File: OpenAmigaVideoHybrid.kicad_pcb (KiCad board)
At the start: 2 copper layers, 56.4 x 21.1 mm, 52 parts, among them J1 Conn_01x22, J99 OSHW_LOGO, Q1 2N3904, Q2 2N3904, Q3 2N3904, Q4 2N3904, Q5 2N3904, Q6 2N3906

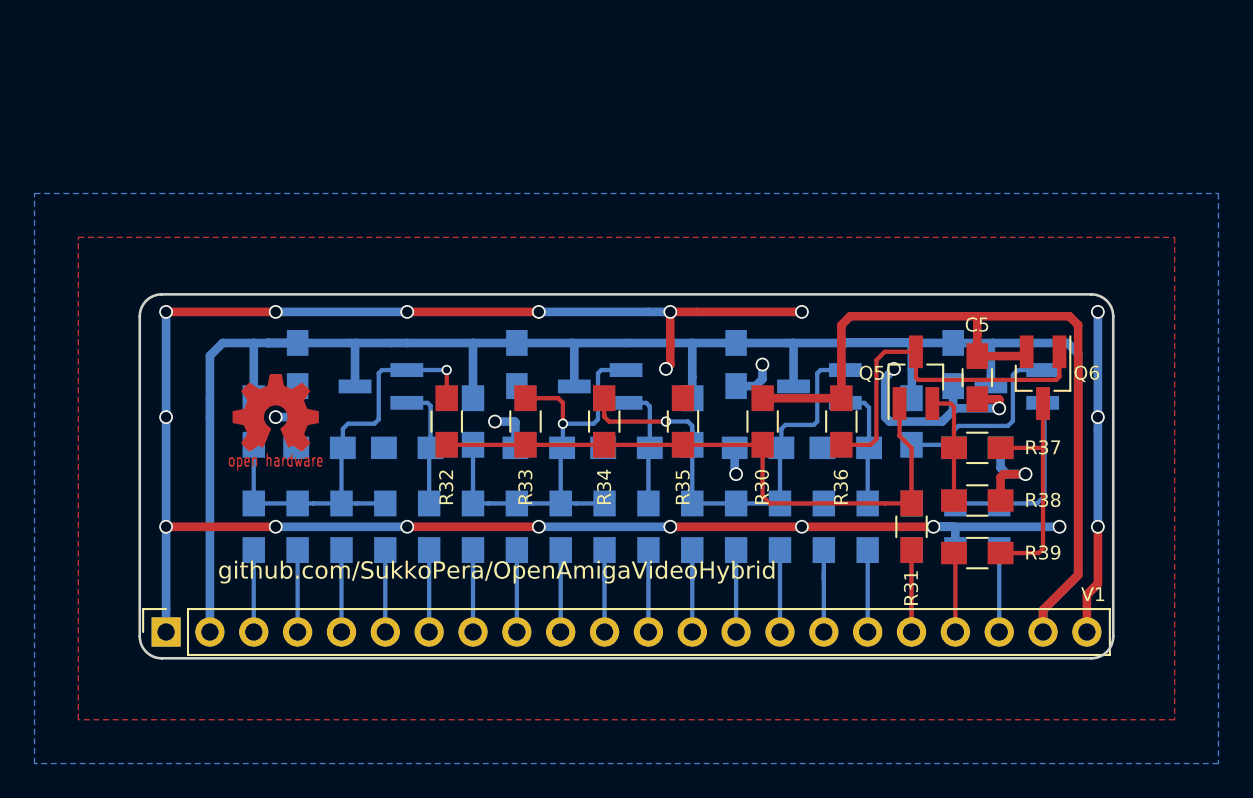
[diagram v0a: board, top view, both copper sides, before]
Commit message: Begin migrating project to KiCad 5
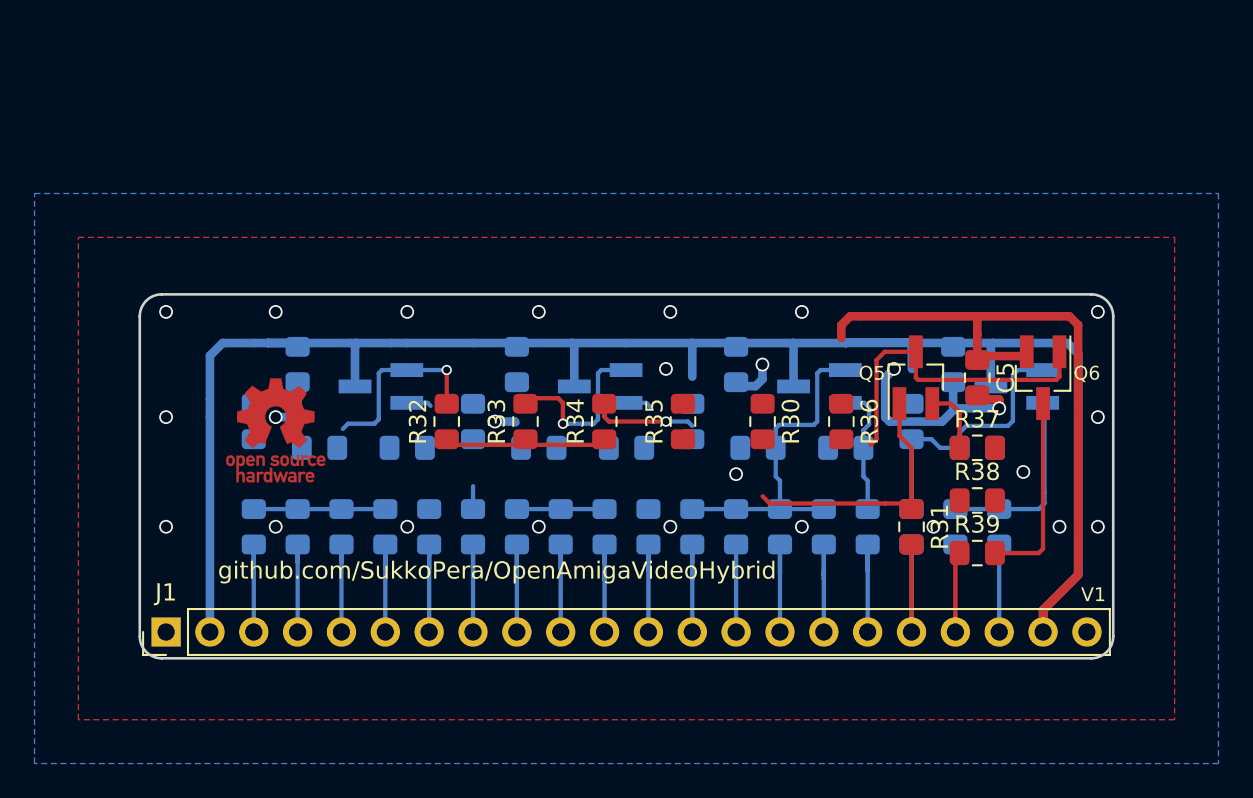
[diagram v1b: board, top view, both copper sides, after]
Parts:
- removed J99: OSHW_LOGO, w_logo:Logo_copper_OSHW_6x6mm
- added V0: OSHW_LOGO, Symbol:OSHW-Logo_5.7x6mm_Copper, F.Cu at (125.7, 112.8)
- C1, C2, C3, C4, C5: footprint Capacitors_SMD:C_0805_HandSoldering -> Capacitor_SMD:C_0805_2012Metric_Pad1.15x1.40mm_HandSolder
- J1: value Conn_01x22 -> CONN_MAINBOARD; footprint OpenAmigaVideoHybrid:Pin_Header_Straight_1x22_Pitch2.54mm -> Connector_PinHeader_2.54mm:PinHeader_1x22_P2.54mm_Vertical; moved to F.Cu
- R1, R10, R11, R12, R13, R14, R15, R16, R17, R18, R19, R2, R20, R21, R22, R23, R24, R25, R26, R27, R28, R29, R3, R30, R31, R32, R33, R34, R35, R36, R37, R38, R39, R4, R5, R6, R7, R8, R9: footprint Resistors_SMD:R_0805_HandSoldering -> Resistor_SMD:R_0805_2012Metric_Pad1.15x1.40mm_HandSolder
- turned J1 to 90 degrees
- turned R22 to 0 degrees
- turned R23 to 0 degrees
- turned R25 to 90 degrees
- turned R27 to 180 degrees
- turned R28 to 90 degrees
- turned R37 to 0 degrees
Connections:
- R13 pad 1: VCC -> Net-(Q2-Pad2)
- R13 pad 2: Net-(Q2-Pad2) -> VCC
- R14 pad 1: Net-(Q2-Pad2) -> GND
- R14 pad 2: GND -> Net-(Q2-Pad2)
- R15 pad 1: Net-(Q2-Pad1) -> GND
- R15 pad 2: GND -> Net-(Q2-Pad1)
- R21 pad 1: VCC -> Net-(Q3-Pad2)
- R21 pad 2: Net-(Q3-Pad2) -> VCC
- R22 pad 1: Net-(Q3-Pad2) -> GND
- R22 pad 2: GND -> Net-(Q3-Pad2)
- R23 pad 1: Net-(Q3-Pad1) -> GND
- R23 pad 2: GND -> Net-(Q3-Pad1)
- R25 pad 1: VCC -> Net-(Q4-Pad2)
- R25 pad 2: Net-(Q4-Pad2) -> VCC
- R27 pad 1: Net-(Q4-Pad2) -> GND
- R27 pad 2: GND -> Net-(Q4-Pad2)
- R28 pad 1: Net-(Q4-Pad1) -> GND
- R28 pad 2: GND -> Net-(Q4-Pad1)
- R30 pad 1: VCC -> Net-(Q5-Pad2)
- R30 pad 2: Net-(Q5-Pad2) -> VCC
- R35 pad 1: Net-(Q5-Pad2) -> GND
- R35 pad 2: GND -> Net-(Q5-Pad2)
- R36 pad 1: VCC -> Net-(Q5-Pad3)
- R36 pad 2: Net-(Q5-Pad3) -> VCC
- R37 pad 1: Net-(Q6-Pad3) -> Net-(Q5-Pad1)
- R37 pad 2: Net-(Q5-Pad1) -> Net-(Q6-Pad3)
- R38 pad 1: Net-(Q5-Pad1) -> GND
- R38 pad 2: GND -> Net-(Q5-Pad1)
- R5 pad 1: VCC -> Net-(Q1-Pad2)
- R5 pad 2: Net-(Q1-Pad2) -> VCC
- R6 pad 1: Net-(Q1-Pad2) -> GND
- R6 pad 2: GND -> Net-(Q1-Pad2)
- R7 pad 1: Net-(Q1-Pad1) -> GND
- R7 pad 2: GND -> Net-(Q1-Pad1)
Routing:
- net GND: track 160.8 -> 19.7 mm
- net VCC: track 159.2 -> 141.8 mm
- net Net-(Q5-Pad2): track 36.1 -> 24.0 mm
- net Net-(Q2-Pad2): track 25.7 -> 16.1 mm
- net Net-(Q1-Pad2): track 26.2 -> 18.5 mm
- net Net-(Q1-Pad1): track 7.13 -> 1.45 mm
- net Net-(Q2-Pad1): track 7.11 -> 1.46 mm
- net Net-(Q3-Pad2): track 30.5 -> 25.9 mm
- net Net-(Q5-Pad1): track 6.75 -> 3.84 mm
- net Net-(Q6-Pad3): track 13.4 -> 11.0 mm
- net /db0: track 5.19 -> 6.96 mm
- net Net-(Q5-Pad3): track 20.6 -> 18.9 mm
- net /db1: track 4.49 -> 6.13 mm
- net /csync: track 9.24 -> 10.9 mm
- net /green: track 4.49 -> 6.01 mm
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
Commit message: Start working on color composite version
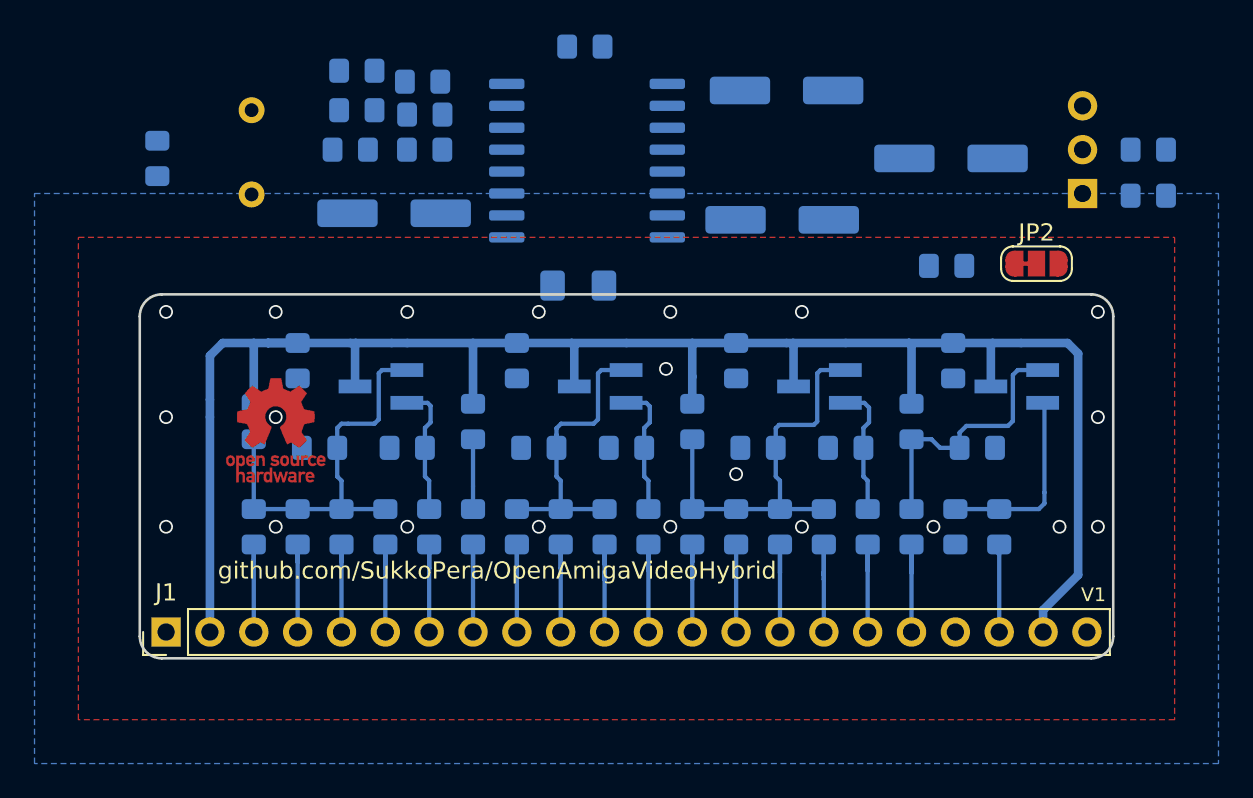
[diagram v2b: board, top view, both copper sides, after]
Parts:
- removed C5: 100n, Capacitor_SMD:C_0805_2012Metric_Pad1.15x1.40mm_HandSolder
- removed Q5: 2N3904, OpenAmigaVideoHybrid:2N3904_2N3906_SOT-23
- removed Q6: 2N3906, OpenAmigaVideoHybrid:2N3904_2N3906_SOT-23
- removed R30: 90.9k, Resistor_SMD:R_0805_2012Metric_Pad1.15x1.40mm_HandSolder
- removed R31, R34: 37.4k, Resistor_SMD:R_0805_2012Metric_Pad1.15x1.40mm_HandSolder
- removed R32: 13.3k, Resistor_SMD:R_0805_2012Metric_Pad1.15x1.40mm_HandSolder
- removed R33: 6.04k, Resistor_SMD:R_0805_2012Metric_Pad1.15x1.40mm_HandSolder
- removed R35: 19.6k, Resistor_SMD:R_0805_2012Metric_Pad1.15x1.40mm_HandSolder
- removed R36: 220, Resistor_SMD:R_0805_2012Metric_Pad1.15x1.40mm_HandSolder
- removed R37, R38: 36, Resistor_SMD:R_0805_2012Metric_Pad1.15x1.40mm_HandSolder
- removed R39: 75, Resistor_SMD:R_0805_2012Metric_Pad1.15x1.40mm_HandSolder
- added C11: 10pF, Capacitor_SMD:C_0805_2012Metric_Pad1.15x1.40mm_HandSolder, B.Cu at (118.9, 97.0)
- added C12: 100n, Capacitor_SMD:C_0805_2012Metric_Pad1.15x1.40mm_HandSolder, B.Cu at (134.4, 96.5)
- added C13: 100n, Capacitor_SMD:C_0805_2012Metric_Pad1.15x1.40mm_HandSolder, B.Cu at (134.4, 94.5)
- added C14: 100n, Capacitor_SMD:C_0805_2012Metric_Pad1.15x1.40mm_HandSolder, B.Cu at (134.2, 92.6)
- added C15: 220u, Capacitor_SMD:CP_Elec_6.3x7.7, B.Cu at (164.8, 97.0)
- added C16: 220u, Capacitor_SMD:CP_Elec_6.3x7.7, B.Cu at (155.1, 100.6)
- added C17: 220u, Capacitor_SMD:CP_Elec_6.3x7.7, B.Cu at (155.3, 93.1)
- added C18: 100n, Capacitor_SMD:C_0805_2012Metric_Pad1.15x1.40mm_HandSolder, B.Cu at (143.6, 90.6)
- added C19: 100u, Capacitor_SMD:CP_Elec_6.3x5.8, B.Cu at (132.6, 100.2)
- added C20: 100n, Capacitor_SMD:C_1206_3216Metric_Pad1.42x1.75mm_HandSolder, B.Cu at (143.3, 104.4)
- added J2: SVIDEO_OUT, Connector_PinHeader_2.54mm:PinHeader_1x03_P2.54mm_Vertical, B.Cu at (172.5, 99.1)
- added JP2: NTSC/~PAL, OpenAmigaVideoHybrid:SolderJumper-3_P1.3mm_Bridged12_RoundedPad1.0x1.5mm, F.Cu at (169.8, 103.1)
- added R40: 75, Resistor_SMD:R_0805_2012Metric_Pad1.15x1.40mm_HandSolder, B.Cu at (130.0, 96.5)
- added R41: 75, Resistor_SMD:R_0805_2012Metric_Pad1.15x1.40mm_HandSolder, B.Cu at (130.4, 94.2)
- added R42: 75, Resistor_SMD:R_0805_2012Metric_Pad1.15x1.40mm_HandSolder, B.Cu at (130.4, 91.9)
- added R43: 75, Resistor_SMD:R_0805_2012Metric_Pad1.15x1.40mm_HandSolder, B.Cu at (164.6, 103.3)
- added R44: 75, Resistor_SMD:R_0805_2012Metric_Pad1.15x1.40mm_HandSolder, B.Cu at (176.3, 99.2)
- added R45: 75, Resistor_SMD:R_0805_2012Metric_Pad1.15x1.40mm_HandSolder, B.Cu at (176.3, 96.5)
- added U2: AD724, Package_SO:SOIC-16W_7.5x10.3mm_P1.27mm, B.Cu at (143.8, 97.2)
- added Y2: 4.433619M, Crystal:Crystal_HC49-4H_Vertical, B.Cu at (124.3, 94.2)
- moved C1 0.22 mm to (127.0, 108.7)
- moved C2 0.22 mm to (139.7, 108.7)
- moved C3 0.22 mm to (152.4, 108.7)
- moved C4 0.22 mm to (165.0, 108.7)
- turned R13 to 90 degrees
- turned R14 to 0 degrees
- turned R15 to 0 degrees
- turned R21 to 90 degrees
- turned R5 to 90 degrees
- turned R6 to 0 degrees
- turned R7 to 0 degrees
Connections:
- net VCC renamed VAA
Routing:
- net VAA: track 141.8 -> 109.7 mm
- net Net-(Q5-Pad2): track 24.0 -> 0.00 mm
- net GND: track 19.7 -> 0.11 mm, vias 26 -> 21
- net Net-(Q5-Pad3): track 18.9 -> 0.00 mm
- net Net-(Q6-Pad3): track 11.0 -> 0.00 mm
- net Net-(Q1-Pad1): track 1.45 -> 7.66 mm
- net Net-(Q2-Pad1): track 1.46 -> 7.64 mm
- net Net-(Q1-Pad2): track 18.5 -> 23.4 mm, vias 1 -> 0
- net /csync: track 10.9 -> 6.13 mm
- net /comp: track 4.61 -> 0.00 mm
- net Net-(Q2-Pad2): track 16.1 -> 20.6 mm, vias 1 -> 0
- net Net-(Q5-Pad1): track 3.84 -> 0.00 mm
- net Net-(Q3-Pad2): track 25.9 -> 23.5 mm, vias 1 -> 0

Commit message: Almost there...
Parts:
- C1, C2, C3, C4, Q1, Q2, Q3, Q4, R1, R10, R11, R12, R13, R14, R15, R16, R17, R18, R19, R2, R20, R21, R22, R23, R24, R25, R26, R27, R28, R29, R3, R4, R5, R6, R7, R8, R9: moved to F.Cu
- JP2, V0: moved to B.Cu
- Y2: footprint Crystal:Crystal_HC49-4H_Vertical -> Crystal:Crystal_SMD_HC49-SD
- moved JP2 35.5 mm to (137.9, 118.7), turned to 270 degrees
- moved Y2 26.5 mm to (129.4, 120.3), turned to 0 degrees
- moved C11 23.6 mm to (132.6, 116.2), turned to 180 degrees
- moved C20 22.7 mm to (122.8, 114.3)
- moved C15 22.0 mm to (168.3, 118.7)
- moved C16 18.4 mm to (158.2, 118.7)
- moved U2 17.3 mm to (146.1, 114.3)
- moved C17 17.1 mm to (158.5, 109.8)
- moved C18 16.9 mm to (145.9, 107.3)
- moved R40 16.1 mm to (132.6, 112.4), turned to 180 degrees
- moved C12 16.1 mm to (136.9, 112.4), turned to 180 degrees
- moved R45 15.9 mm to (167.6, 109.8), turned to 180 degrees
- moved R41 15.8 mm to (132.6, 109.8), turned to 180 degrees
- moved C13 15.6 mm to (136.9, 109.8), turned to 180 degrees
- moved R42 15.5 mm to (132.6, 107.3), turned to 180 degrees
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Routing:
- net VAA: track 109.7 -> 184.2 mm
- net /blue: track 6.01 -> 61.5 mm
- net /green: track 6.01 -> 47.5 mm
- net /red: track 5.88 -> 30.5 mm
- net /comp: track 0.00 -> 22.7 mm
- net /composite: track 0.00 -> 19.8 mm
- net /csync: track 6.13 -> 20.9 mm
- net Net-(C11-Pad1): track 0.00 -> 11.8 mm
- net /luma: track 0.00 -> 10.6 mm
- net Net-(C15-Pad2): track 0.00 -> 9.87 mm
- net Net-(C17-Pad2): track 0.00 -> 5.42 mm
- net /chroma: track 0.00 -> 5.10 mm
- net Net-(C14-Pad1): track 0.00 -> 4.60 mm
- net Net-(C13-Pad1): track 0.00 -> 4.08 mm
- net Net-(JP2-Pad2): track 0.00 -> 3.47 mm
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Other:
- board size 56.4 x 21.1 mm -> 56.4 x 21.5 mm
- board text added: "NTSC"
- board text added: "PAL"

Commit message: Even closer...
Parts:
- moved C15 10.0 mm to (158.2, 118.7)
- moved C16 10.0 mm to (168.3, 118.7)
- moved R44 5.08 mm to (167.6, 112.4)
- moved R45 2.54 mm to (167.6, 107.3)
- moved R43 2.54 mm to (167.6, 109.8)
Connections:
- R44 pad 1: Net-(J2-Pad1) -> Net-(J2-Pad2)
- R45 pad 1: Net-(J2-Pad2) -> Net-(J2-Pad1)
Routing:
- net /luma: track 10.6 -> 23.2 mm
- net /composite: track 19.8 -> 11.1 mm
- net Net-(C16-Pad2): track 0.00 -> 8.16 mm
- net /comp: track 22.7 -> 28.9 mm
- net Net-(C15-Pad2): track 9.87 -> 12.5 mm
- net Net-(C17-Pad2): track 5.42 -> 7.53 mm
- net Net-(J2-Pad2): track 2.91 -> 4.84 mm

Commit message: THERE! Just needs some polishing!
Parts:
- V0: moved to F.Cu
- moved V0 58.1 mm to (171.1, 119.3)
- moved C4 2.54 mm to (162.4, 108.7)
- moved Q2 2.54 mm to (142.0, 110.2)
- moved R11 2.54 mm to (139.7, 118.4)
- moved R15 2.54 mm to (143.5, 113.8)
- moved R17 2.54 mm to (147.3, 118.4)
- moved R21 2.54 mm to (147.3, 112.3)
- moved R24 2.54 mm to (157.5, 118.4)
- moved R4 2.54 mm to (129.5, 118.4)
- moved C1 2.54 mm to (124.5, 108.7)
- moved R2 2.54 mm to (124.5, 118.4)
- moved R6 2.54 mm to (125.7, 113.8)
- moved C2 2.54 mm to (137.2, 108.7)
- moved C3 2.54 mm to (149.9, 108.7)
- moved Q1 2.54 mm to (129.3, 110.2)
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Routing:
- net Net-(Q4-Pad1): track 8.88 -> 15.0 mm
- net VAA: track 184.2 -> 189.6 mm
- net /blue: track 61.5 -> 64.5 mm
- net /sync: track 4.61 -> 6.12 mm
- net /db0: track 6.96 -> 6.12 mm
- net /dr3: track 5.37 -> 6.12 mm
- net /dr2: track 5.50 -> 6.12 mm
- net /dr1: track 5.50 -> 6.12 mm
- net /db2: track 5.50 -> 6.12 mm
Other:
- board text added: "V2"
- board text removed: "V1"

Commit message: Polish hybrid side
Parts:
- V0: footprint Symbol:OSHW-Logo_5.7x6mm_Copper -> OpenAmigaVideoHybrid:oshw_logo
- moved V0 1.65 mm to (171.1, 120.9)
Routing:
- net Net-(Q4-Pad1): track 15.0 -> 14.5 mm
- net GND: vias 0 -> 3
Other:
- board text added: "Licensed under CERN OHL v.1.2"

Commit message: Getting closer...
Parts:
- J2: footprint Connector_PinHeader_2.54mm:PinHeader_1x03_P2.54mm_Vertical -> OpenAmigaVideoHybrid:Pin_Header_Straight_1x03-ModSilkS
- moved R32 8.20 mm to (137.2, 114.1), turned to 0 degrees
- moved C12 6.20 mm to (132.6, 107.9)
- moved C14 4.74 mm to (137.2, 112.0)
- moved R31 4.59 mm to (137.2, 110.0), turned to 0 degrees
- moved R30 2.43 mm to (132.6, 110.0), turned to 0 degrees
- moved C13 1.99 mm to (137.2, 107.9)
- moved C17 0.76 mm to (157.7, 109.8)
- moved C18 0.58 mm to (145.9, 107.9)
- moved C15 0.57 mm to (157.7, 118.5)
- moved R33 0.25 mm to (167.4, 109.9)
- moved C16 0.25 mm to (168.3, 118.5)
- moved C19 0.25 mm to (123.1, 109.1)
- moved C20 0.25 mm to (123.1, 114.3)
- moved R34 0.25 mm to (167.4, 112.4)
- moved R35 0.25 mm to (167.4, 107.3)
- renumbered JP2 to JP1, R40 to R30, R41 to R31, R42 to R32, R43 to R33, R44 to R34, R45 to R35, U2 to U1
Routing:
- net Net-(C12-Pad1): track 3.47 -> 17.5 mm
- net /blue: track 64.5 -> 52.7 mm
- net Net-(C13-Pad1): track 4.08 -> 8.75 mm
- net /green: track 47.6 -> 43.5 mm
- net /red: track 30.8 -> 28.3 mm
- net VAA: track 189.7 -> 188.1 mm
- net /luma: track 23.2 -> 24.6 mm
- net Net-(C14-Pad1): track 4.60 -> 5.72 mm
- net /comp: track 28.9 -> 27.8 mm
- net Net-(C15-Pad2): track 12.5 -> 11.5 mm
- net Net-(C17-Pad2): track 7.53 -> 8.29 mm
- net Net-(J2-Pad2): track 4.84 -> 5.35 mm
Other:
- board size 56.4 x 21.5 mm -> 56.4 x 21.2 mm
- board text added: "C"
- board text added: "G"
- board text added: "L"
